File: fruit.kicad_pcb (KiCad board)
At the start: 4 copper layers, 161.6 x 100 mm, 218 parts, among them J1 PCB_Edge_PCI_Express_x4_Salmo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, J2 2086581051, J3 TSM-102-01-L-SV, J4 TSM-102-01-L-SV, J5 MEM2067-02-180-00-A_REVB, J6 USB4110-GF-A, J7 USB4110-GF-A, J8 1-2199119-6, Q1 MMBT2222AM3T5G, U1 INA260, U10 MCP9808T-E_MC, U11 ADS7142IRUGR, U12 MCP9808T-E_MC, U13 LM3525M-H_NPOB, U14 USB3740B-AI2, U15 AP22653FDZ-7, U16 AP64501SP-13, U17 AP64501SP-13, U2 PCA9671BS,118, U3 SN74LVC1G04DRY, U4 SN74LVC1G07DRY, U5 SN74HCS244, U6 PCA9641BSHP, U7 AP22653FDZ-7, U8 TPD8S009DSMR, U9 INA260

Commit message: dp routing
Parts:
- added CM1: ComputeModule4-CM4, Connector_RaspberryPi:Raspberry-Pi-4-Compute-Module_outline, F.Cu at (121.4, 21.8)
- added COOLER1: 53-61mm_NorthBridge_45deg_arms, Mechanical_CoolingBlock:53-61mm_NorthBridge_45deg_arms, F.Cu at (104.9, 50.3)
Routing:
- net /CM4/PCIE_TX-: track 87.4 -> 89.2 mm
- net /CM4/PCIE_TX+: track 88.2 -> 89.8 mm
- net /EthC-: track 51.6 -> 52.3 mm
- net /EthC+: track 52.6 -> 53.2 mm
- net GND: vias 75 -> 120
- added copper zone on F.Cu, net (none)
- added copper zone on F.Cu, net /CM4/CM4_+3.3V

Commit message: connecterized faceplate, refreshed schematic
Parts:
- removed the C26 at (-29.0, 77.9)
- removed the C29 at (-16.3, 90.9)
- removed the C6 at (179.7, -42.2)
- removed the D1 at (104.5, -47.5)
- removed the D2 at (101.8, -41.2)
- removed the D3 at (97.8, -38.6)
- removed D4: LED Yellow, LED_SMD_LiteOn:LED_0603_1608Metric_yellow
- removed D5: LED Green, LED_SMD_LiteOn:LED_0603_1608Metric_green
- removed D6: LED Orange, LED_SMD_LiteOn:LED_0603_1608Metric_orange
- removed the J5 at (-58.5, 54.1)
- removed the J6 at (-11.0, 75.1)
- removed LED1: APHB1608CGKSEKC_KNB, LED_SMD_Kingbright:APHB1608CGKSEKC
- removed the R50 at (-9.03, 96.5)
- removed the R55 at (-18.3, 88.0)
- removed the U4 at (177.1, -37.8)
- added J3: PicoBlade_1x11_533981171_SMT, Connector_PicoBlade_Molex:MOLEX_533981171, F.Cu at (-93.4, 18.4)
- added J4: PicoBlade_1x6_533980671_SMT, Connector_PicoBlade_Molex:MOLEX_533980671, F.Cu at (-96.5, 23.7)
- added J8: PicoBlade_1x6_533980671_SMT, Connector_PicoBlade_Molex:MOLEX_533980671, F.Cu at (-108.7, 38.8)
- added J9: PicoBlade_1x6_533980671_SMT, Connector_PicoBlade_Molex:MOLEX_533980671, F.Cu at (-108.7, 45.3)
- J2: value 2086581051 -> PicoBlade_1x12_533981371_SMT; footprint Connector_HDMI_Molex:2086581051 -> Connector_PicoBlade_Molex:MOLEX_533981271
- J7: value USB4110-GF-A -> PicoBlade_1x8_533980871_SMT; footprint Connector_USB_GCT:USB4110-GF-A -> Connector_PicoBlade_Molex:MOLEX_533980871
- moved J7 88.2 mm to (-107.5, 58.0), turned to 0 degrees
- moved J2 56.1 mm to (-42.6, 5.00), turned to 90 degrees
- moved C1 10.3 mm to (111.2, 234.2)
- moved TP1 10.3 mm to (111.3, 231.6)
- moved C2 2.02 mm to (114.3, 231.1)
- moved U1 1.04 mm to (105.4, 233.4)
- renumbered C11 to C10, C12 to C11, C13 to C12, C14 to C13, C15 to C14, C16 to C15, C17 to C16, C18 to C17, C19 to C18, C20 to C19, C21 to C20, C22 to C21, C23 to C22, C24 to C23, C25 to C24, C27 to C25, C28 to C26, C30 to C27, C31 to C28, C32 to C29, C33 to C30, C34 to C31, C35 to C32, C36 to C33, C37 to C34, C38 to C35, C39 to C36, C40 to C37, C41 to C38, C42 to C39, C43 to C40, C44 to C41, C45 to C42, C47 to C44, C48 to C45, C49 to C46, C50 to C47, C51 to C48, C52 to C49, C53 to C50, C54 to C51, C55 to C52, C56 to C53, C57 to C54, C58 to C55, C59 to C56, C60 to C57, C61 to C58, C7 to C6, C63 to C60, C64 to C61, C65 to C62, C66 to C63, C67 to C64, C68 to C65, C69 to C66, C70 to C67, C71 to C68, C72 to C69, C8 to C7, C73 to C70, C74 to C71, C75 to C72, C76 to C73, C77 to C74, C78 to C75, C9 to C8, C10 to C9, D7 to D1, D8 to D2, D9 to D3, J8 to J10, J3 to J5, J4 to J6, R51 to R50, R52 to R51, R53 to R52, R54 to R53, R56 to R54, R57 to R55, R58 to R56, R59 to R57, R60 to R58, R61 to R59, R62 to R60, R63 to R61, R64 to R62, R65 to R63, R66 to R64, R67 to R65, R68 to R66, R69 to R67, R70 to R68, R71 to R69, R72 to R70, R73 to R71, R74 to R72, R75 to R73, R76 to R74, R77 to R75, R78 to R76, R79 to R77, R80 to R78, R81 to R79, R82 to R80, U11 to U10, U12 to U11, U13 to U12, U14 to U13, U15 to U14, U16 to U15, U17 to U16, U5 to U4, U6 to U5, U7 to U6, U8 to U7, U9 to U8, U10 to U9
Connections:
- C11 pad 1: /CM4/HDMI/HDMI_+5V -> GND
- C12 pad 1: /CM4/HDMI/HDMI_+5V -> GND
- D1 pad 2: Net-(D7-Pad2) -> /CM4/LED_USB_OTG_CONN
- J2 pad 1: /CM4/HDMID2+ -> /CM4/~{M.2_LED_CONN}
- J2 pad 10: /CM4/HDMICK+ -> /CM4/LED_USB_OTG_CONN
- J2 pad 11: GND -> /CM4/CM4_+3.3V
- J2 pad 12: /CM4/HDMICK- -> GND
- J2 pad 2: GND -> /CM4/~{LED_PWR_LED_BUFFERED_CONN}
- J2 pad 3: /CM4/HDMID2- -> /CM4/~{LED_PI_Activity_CONN}
- J2 pad 4: /CM4/HDMID1+ -> /CM4/~{LED_EthLED1_CONN}
- J2 pad 5: GND -> /CM4/~{LED_EthLED2_CONN}
- J2 pad 6: /CM4/HDMID1- -> /CM4/~{LED_EthLED3_CONN}
- J2 pad 7: /CM4/HDMID0+ -> /CM4/LED_+3.3V_ON_CONN
- J2 pad 8: GND -> /CM4/LED_I2C_PING_1_CONN
- J2 pad 9: /CM4/HDMID0- -> +12V
- Q1 pad 3: Net-(LED1-Pad2) -> Net-(Q1-Pad3)
- R17 pad 2: Net-(LED1-Pad2) -> Net-(Q1-Pad3)
- R18 pad 1: Net-(LED1-Pad3) -> /CM4/LED_+3.3V_ON_CONN
- R19 pad 1: Net-(LED1-Pad1) -> /CM4/LED_I2C_PING_1_CONN
- R19 pad 2: +12V -> Net-(Q1-Pad3)
- R28 pad 1: /CM4/~{I2C_RESET_1_1} -> /CM4/~{I2C_RESET_CM4}
- R4 pad 1: Net-(D1-Pad2) -> /CM4/~{M.2_LED_CONN}
- R5 pad 1: Net-(D2-Pad2) -> /CM4/~{LED_PWR_LED_BUFFERED_CONN}
- R5 pad 2: /CM4/CM4_+3.3V -> /CM4/~{PWR_LED_BUFFERED}
- R50 pad 1: Net-(J6-PadA5) -> /CM4/USB 2.0 MUX/USB1_CC1
- R53 pad 1: Net-(D7-Pad2) -> /CM4/LED_USB_OTG_CONN
- R54 pad 1: Net-(J7-PadA5) -> /CM4/USB 2.0 MUX/USB2_CC1
- R6 pad 1: Net-(D3-Pad2) -> /CM4/~{LED_PI_Activity_CONN}
- R6 pad 2: /CM4/CM4_+3.3V -> /CM4/~{PI_Activity}
- R7 pad 1: /CM4/CM4_+3.3V -> /CM4/~{EthLED1}
- R7 pad 2: Net-(D4-Pad2) -> /CM4/~{LED_EthLED1_CONN}
- R8 pad 1: /CM4/CM4_+3.3V -> /CM4/~{EthLED2}
- R8 pad 2: Net-(D5-Pad2) -> /CM4/~{LED_EthLED2_CONN}
- R9 pad 1: /CM4/CM4_+3.3V -> /CM4/~{EthLED3}
- R9 pad 2: Net-(D6-Pad2) -> /CM4/~{LED_EthLED3_CONN}
- TP3 pad 1: Net-(C6-Pad1) -> /CM4/~{PWR_LED_BUFFERED}
- TP9 pad 1: Net-(LED1-Pad2) -> Net-(Q1-Pad3)
- U4 pad 10: ePAD -> GND
- U4 pad 15: ePAD -> GND
- U4 pad 17: ePAD -> /CM4/~{PWR_LED}
- U4 pad 21: ePAD -> GND
- U4 pad 3: unconnected-(U5-Pad3) -> /CM4/~{PWR_LED_BUFFERED}
- U4 pad 6: ePAD -> GND
- U4 pad 8: ePAD -> GND
- U6 pad 6: /CM4/HDMI/HDMI_+5V -> GND

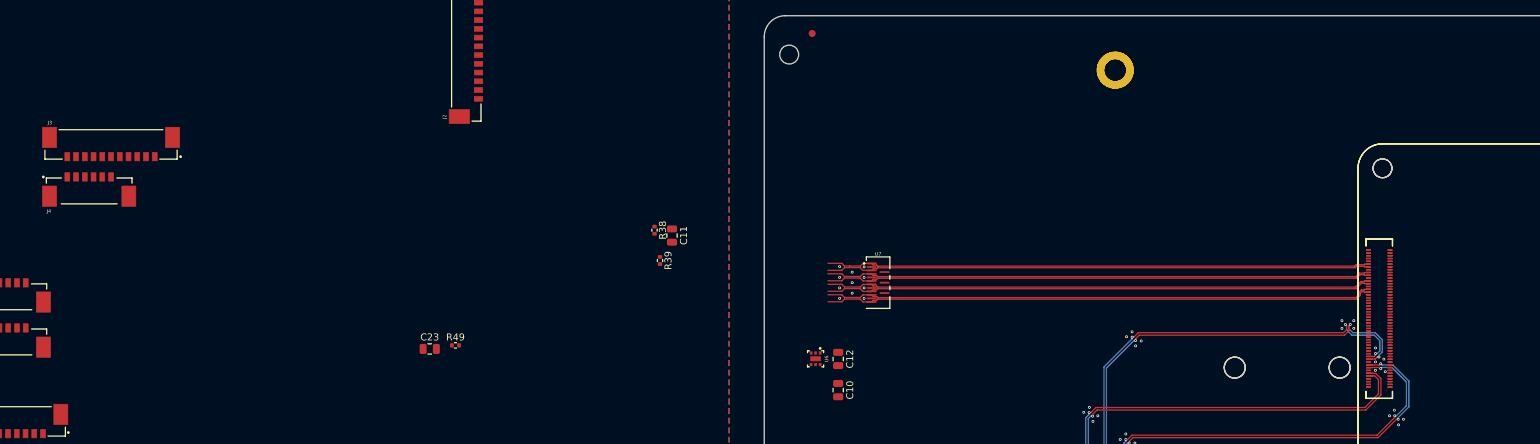
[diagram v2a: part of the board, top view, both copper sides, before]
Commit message: placed hdmi conn
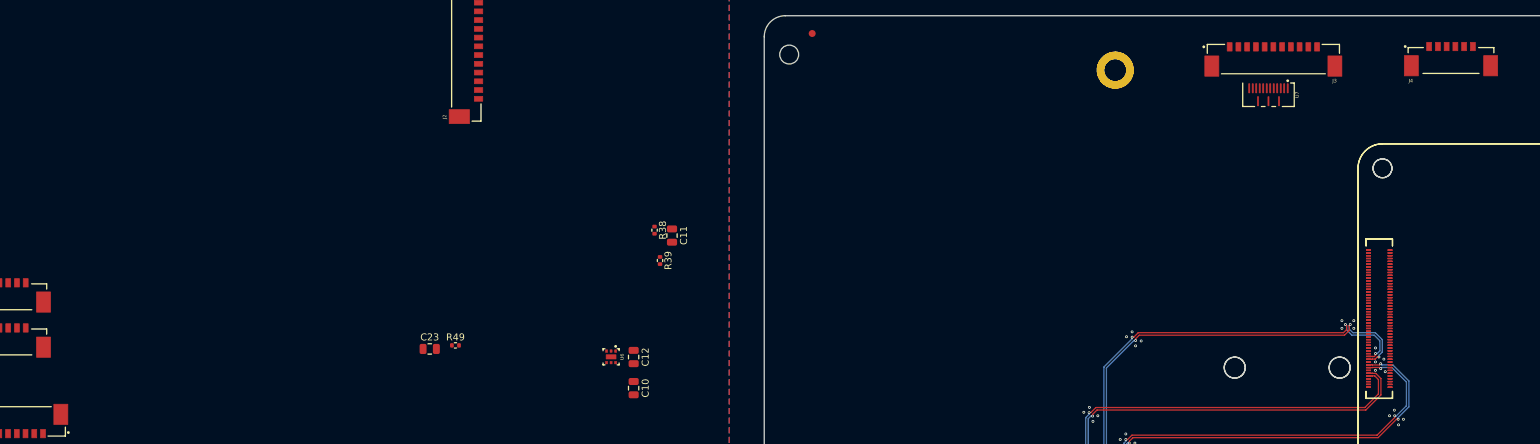
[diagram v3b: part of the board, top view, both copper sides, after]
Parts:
- moved J4 195.6 mm to (98.2, 5.05)
- moved J3 166.6 mm to (72.8, 6.20), turned to 180 degrees
- moved U7 61.9 mm to (72.1, 11.3), turned to -90 degrees
- moved C10 29.2 mm to (-18.7, 53.2)
- moved C12 29.2 mm to (-18.7, 48.8)
- moved U6 29.2 mm to (-21.9, 48.8)
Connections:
- J3 pad 1: /CM4/HDMID0+ -> /CM4/HDMID2+
- J3 pad 2: /CM4/HDMID0- -> /CM4/HDMID2-
- J3 pad 7: /CM4/HDMID2+ -> /CM4/HDMID0+
- J3 pad 8: /CM4/HDMID2- -> /CM4/HDMID0-
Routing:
- net /CM4/HDMID2+: track 78.4 -> 0.00 mm
- net /CM4/HDMID2-: track 78.4 -> 0.00 mm
- net /CM4/HDMID1+: track 78.1 -> 0.00 mm
- net /CM4/HDMID1-: track 78.1 -> 0.00 mm
- net /CM4/HDMID0+: track 78.0 -> 0.00 mm
- net /CM4/HDMID0-: track 78.0 -> 0.00 mm
- net /CM4/HDMICK+: track 77.9 -> 0.00 mm
- net /CM4/HDMICK-: track 77.9 -> 0.00 mm
- net GND: vias 120 -> 109

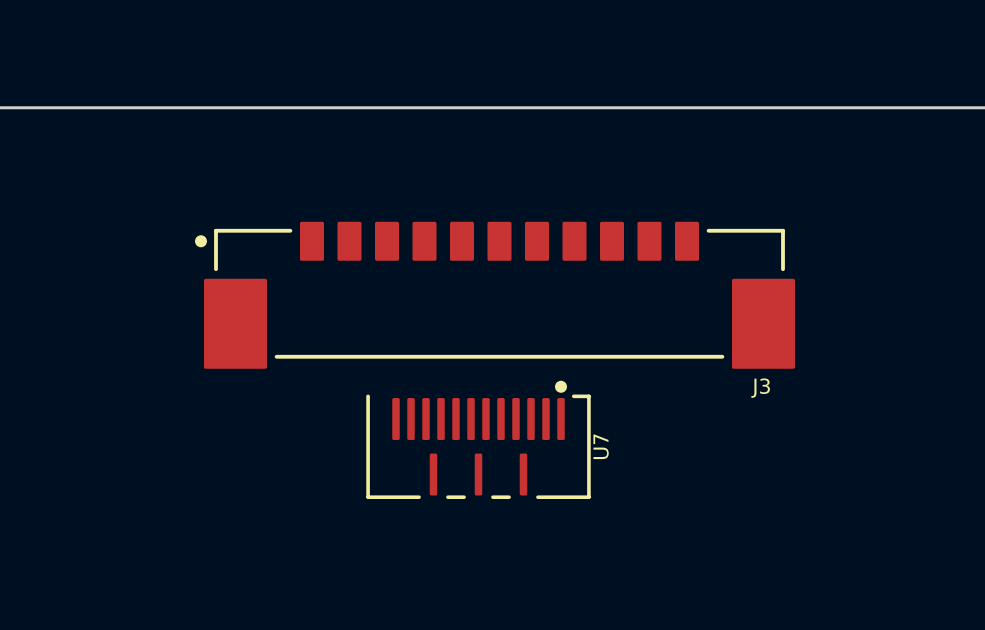
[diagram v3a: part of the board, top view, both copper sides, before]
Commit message: hdmi dp routing
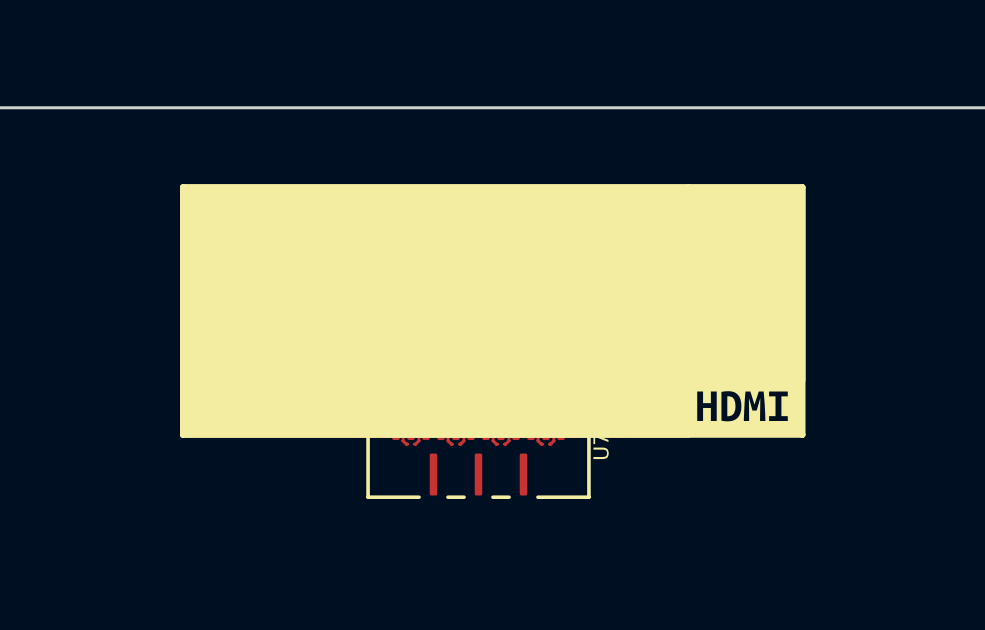
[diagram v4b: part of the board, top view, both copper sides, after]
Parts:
- added kibuzzard-61E484E1: G***, kibuzzard-61E484E1, F.Cu at (80.9, 9.95)
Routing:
- net /CM4/HDMICK-: track 0.00 -> 10.0 mm
- net /CM4/HDMICK+: track 0.00 -> 10.0 mm
- net /CM4/HDMID2-: track 0.00 -> 8.89 mm
- net /CM4/HDMID2+: track 0.00 -> 8.89 mm
- net /CM4/HDMID0-: track 0.00 -> 8.07 mm
- net /CM4/HDMID0+: track 0.00 -> 8.07 mm
- net /CM4/HDMID1-: track 0.00 -> 7.49 mm
- net /CM4/HDMID1+: track 0.00 -> 7.49 mm
- net GND: vias 109 -> 113

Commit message: hdmi dp routed
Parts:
- COOLER1 (x2): value 53-61mm_NorthBridge_45deg_arms -> 53-61
- Q1: value MMBT2222AM3T5G -> SOT-723_0P85X1P25_ONS
- U10: value ADS7142IRUGR -> RUG0010A
- moved J7 222.7 mm to (109.2, 6.30)
- moved J4 7.90 mm to (90.3, 5.10)
- moved kibuzzard-61E484E1 2.15 mm to (83.0, 9.95)
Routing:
- net /CM4/HDMID2+: track 8.89 -> 57.7 mm
- net /CM4/HDMID2-: track 8.89 -> 57.3 mm
- net /CM4/HDMID1+: track 7.49 -> 54.0 mm
- net /CM4/HDMID1-: track 7.49 -> 53.6 mm
- net /CM4/HDMID0+: track 8.07 -> 51.6 mm
- net /CM4/HDMID0-: track 8.07 -> 51.2 mm
- net /CM4/HDMICK+: track 10.0 -> 51.2 mm
- net /CM4/HDMICK-: track 10.0 -> 50.9 mm

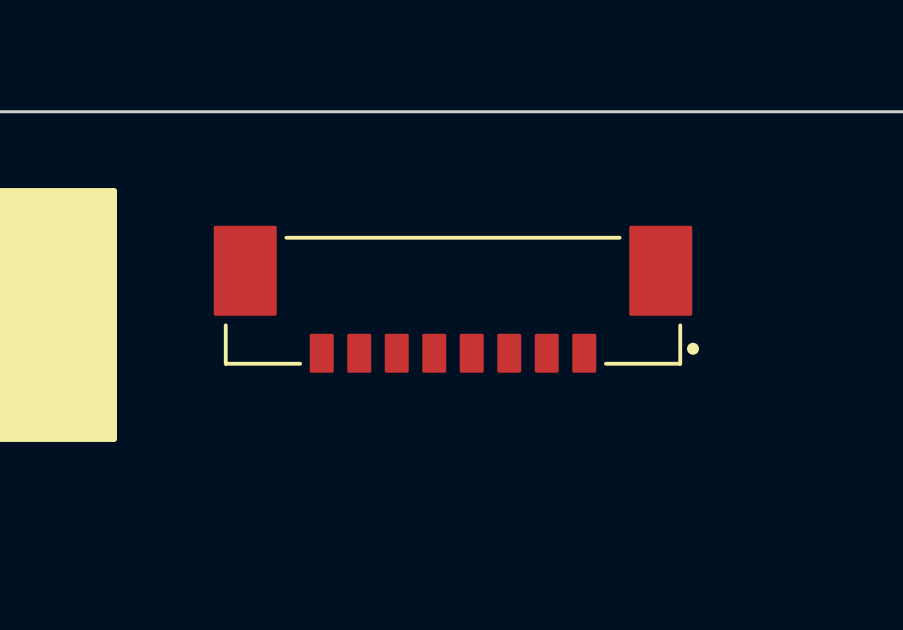
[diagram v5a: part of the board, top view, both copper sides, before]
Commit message: microsd conn placed
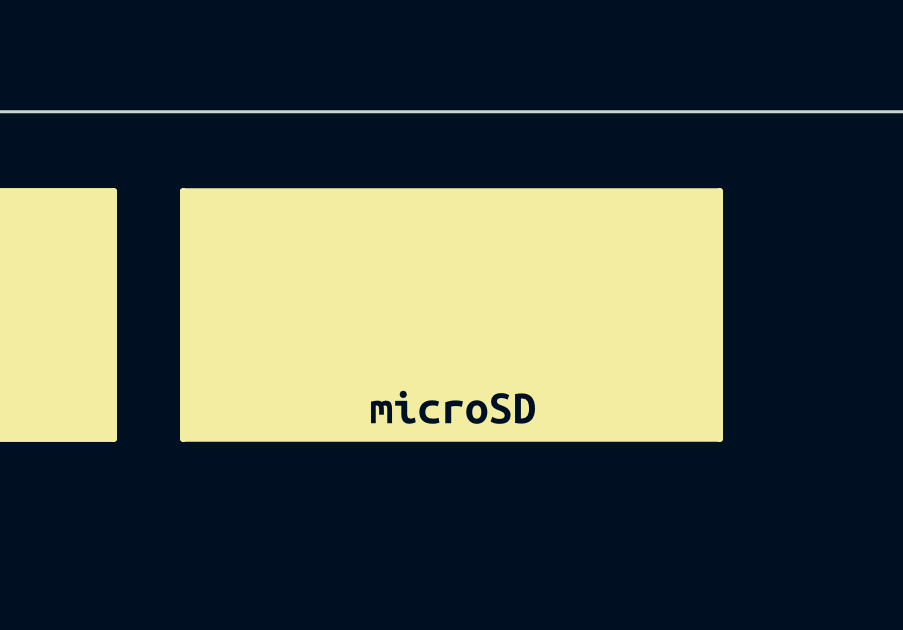
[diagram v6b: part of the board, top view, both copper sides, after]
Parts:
- added kibuzzard-61E49B53: G***, kibuzzard-61E49B53, F.Cu at (109.2, 9.85)
